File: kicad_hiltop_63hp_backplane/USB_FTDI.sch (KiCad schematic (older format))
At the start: 53 parts, among them J1 USB_B_Micro, J2 3pos_Jumper, J3 3pos_Jumper, U1 93LCxxC, U2 FT2232H, Y1 ABM10AIG-12.000MHZ-4Z-T3

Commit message: add latest changes
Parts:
- removed C1: 100nF, Capacitor_SMD:C_0402_1005Metric, symbol hiltop_backplane_brd-rescue:C-device
- removed D1: MBR230LSFT1G, Diode_SMD:D_SOD-123F, symbol hiltop_backplane_brd-rescue:D_Schottky-device
- removed D2: NUP2105L, Package_TO_SOT_SMD:SOT-23, symbol hiltop_backplane_brd-rescue:NUP2105L-ESD_Protection
- removed J1: USB_B_Micro, Connector_USB:USB_Micro-B_GCT_USB3076-30-A, symbol Connector:USB_B_Micro
- removed J2, J3: 3pos_Jumper, GTI_Footprint_Lib:3POS_JUMPER_R_0603_1608Metric, symbol hiltop_backplane_brd-rescue:3pos_Jumper-gti_Lattice
- removed L1: Ferrite_Bead, Inductor_SMD:L_0603_1608Metric, symbol hiltop_backplane_brd-rescue:Ferrite_Bead-device
- removed R5, R6: 0, Resistor_SMD:R_0402_1005Metric, symbol hiltop_backplane_brd-rescue:R-device
- removed TP14: Test_Point, TestPoint:TestPoint_Pad_D1.0mm, symbol hiltop_backplane_brd-rescue:TestPoint-Connector
- C10, C11, C12, C13, C14, C15, C16, C17, C18, C19, C2, C3, C4, C5, C6, C7, C8, C9: symbol hiltop_backplane_brd-rescue:C-device -> hiltop_backplane_brd-rescue:C-device-hiltop_backplane_brd-rescue
- D3, D4: symbol hiltop_backplane_brd-rescue:LED-device -> hiltop_backplane_brd-rescue:LED-device-hiltop_backplane_brd-rescue
- L2, L3, L4, L5: symbol hiltop_backplane_brd-rescue:Ferrite_Bead-device -> hiltop_backplane_brd-rescue:Ferrite_Bead-device-hiltop_backplane_brd-rescue
- R1, R10, R11, R12, R13, R14, R15, R16, R17, R2, R3, R4, R7, R8, R9: symbol hiltop_backplane_brd-rescue:R-device -> hiltop_backplane_brd-rescue:R-device-hiltop_backplane_brd-rescue
- TP15: symbol hiltop_backplane_brd-rescue:TestPoint-Connector -> hiltop_backplane_brd-rescue:TestPoint-Connector-hiltop_backplane_brd-rescue
- U1: symbol hiltop_backplane_brd-rescue:93LCxxC-memory -> hiltop_backplane_brd-rescue:93LCxxC-memory-hiltop_backplane_brd-rescue
- U2: symbol hiltop_backplane_brd-rescue:FT2232H-gti_Lattice -> hiltop_backplane_brd-rescue:FT2232H-gti_Lattice-hiltop_backplane_brd-rescue
- Y1: symbol hiltop_backplane_brd-rescue:Crystal_GND24-device -> hiltop_backplane_brd-rescue:Crystal_GND24-device-hiltop_backplane_brd-rescue
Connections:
- net labels removed: USB_D+, USB_D-
- wire segments 237 -> 218
- no-connect marks 22 -> 21
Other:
- note removed: "4.7V from USB"

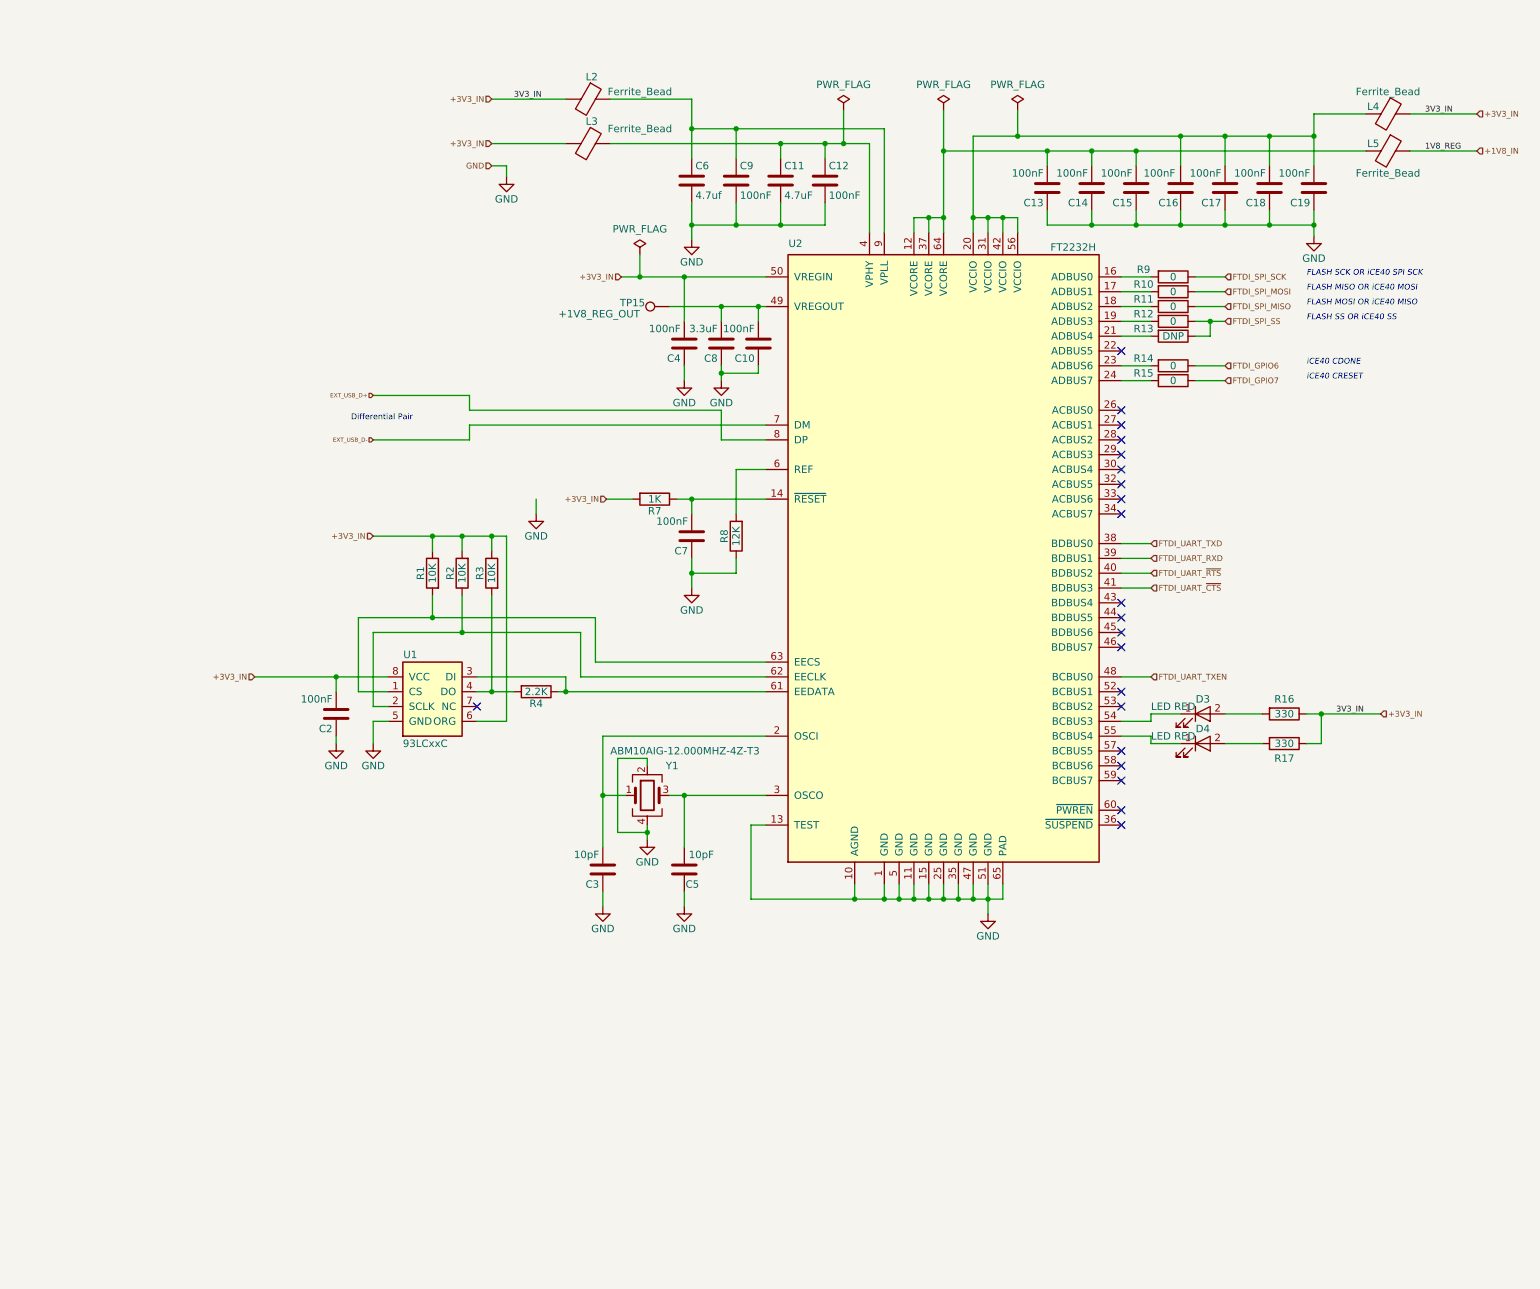
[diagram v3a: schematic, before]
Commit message: updated schematics to RevC including general tidy up
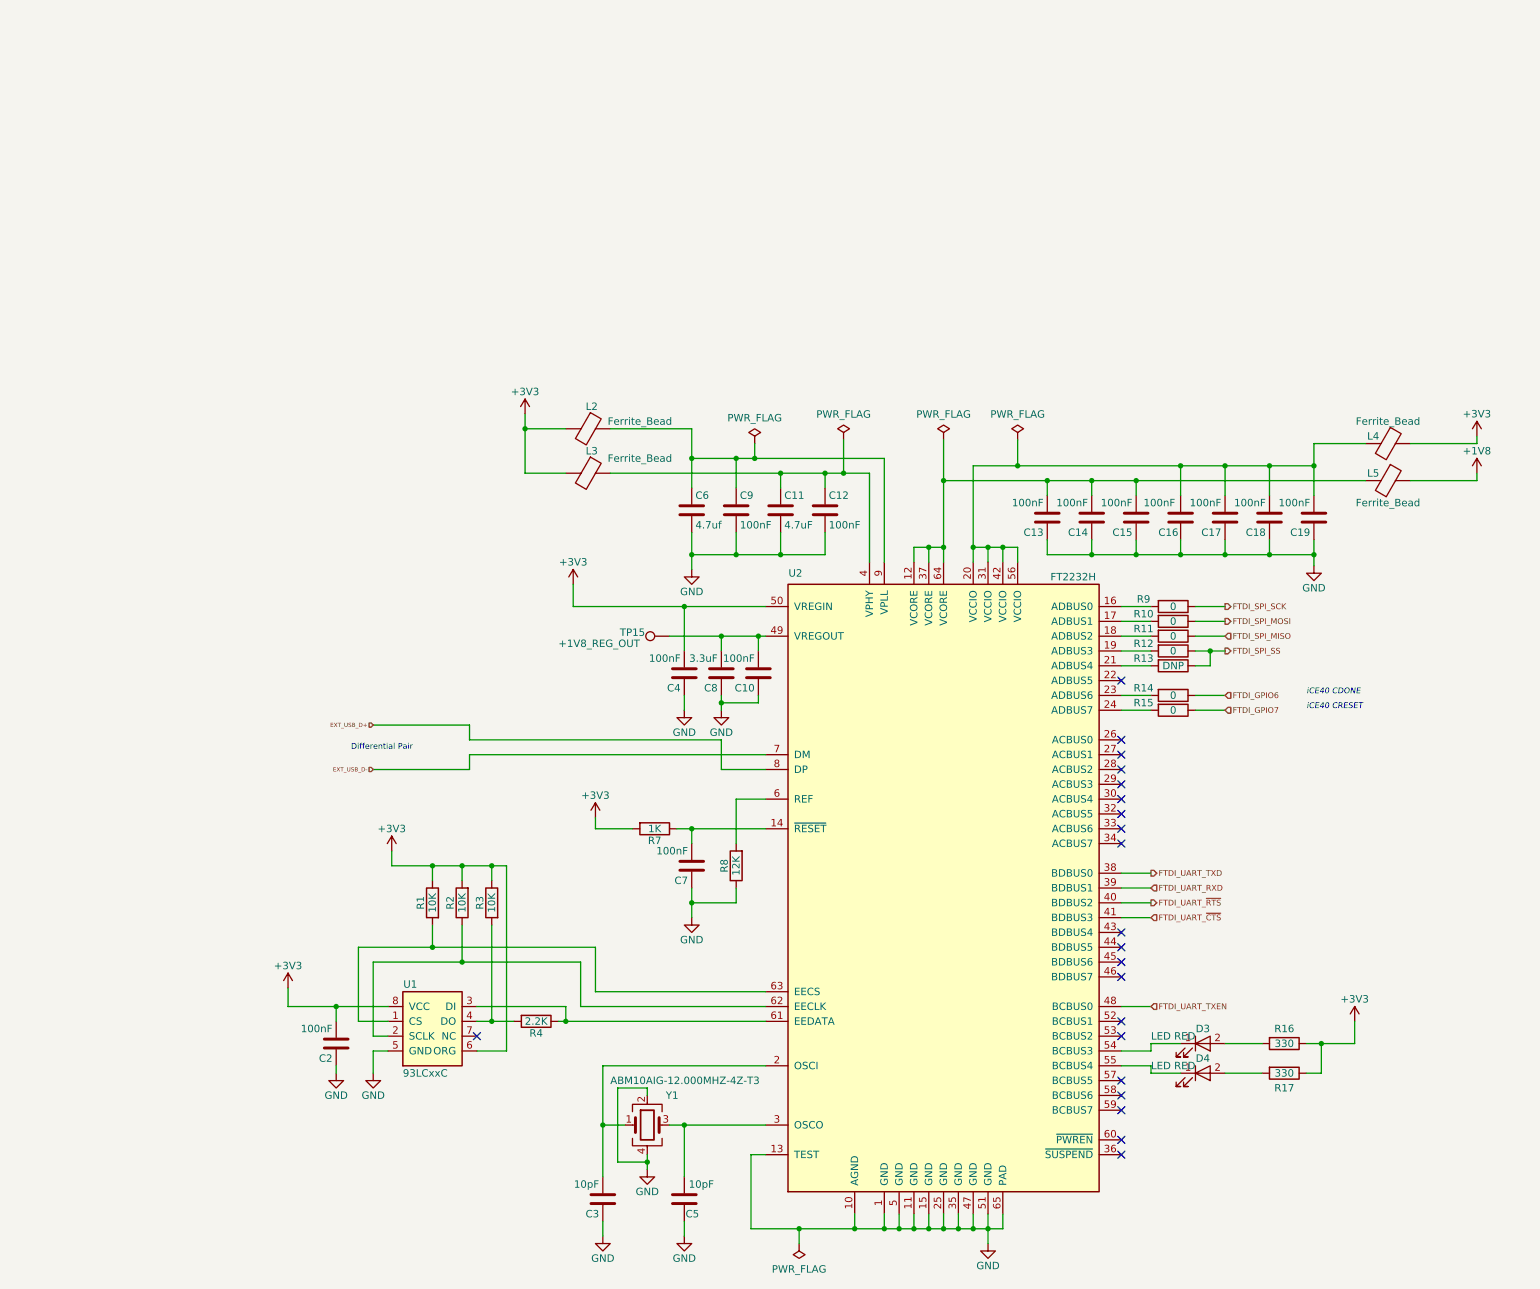
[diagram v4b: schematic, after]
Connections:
- net +1V8_IN renamed +1V8
- net +3V3_IN renamed +3V3
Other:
- note removed: "FLASH MISO OR iCE40 MOSI"
- note removed: "FLASH MOSI OR iCE40 MISO"
- note removed: "FLASH SCK OR iCE40 SPI SCK"
- note removed: "FLASH SS OR iCE40 SS"
- moved on the sheet: C10, C11, C12, C13, C14, C15, C16, C17, C18, C19, C2, C3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

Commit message: updated backplane connector details
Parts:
- TP15: footprint TestPoint:TestPoint_Pad_D1.0mm -> TestPoint:TestPoint_THTPad_D1.0mm_Drill0.5mm
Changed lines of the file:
@@
 F 0 "TP15" V 5425 4525 50  0000 C CNN
 F 1 "+1V8_REG_OUT" V 5350 4750 50  0000 C CNN
-F 2 "TestPoint:TestPoint_Pad_D1.0mm" H 5600 4275 50  0001 C CNN
+F 2 "TestPoint:TestPoint_THTPad_D1.0mm_Drill0.5mm" H 5600 4275 50  0001 C CNN
 F 3 "~" H 5600 4275 50  0001 C CNN
 	1    5400 4275
